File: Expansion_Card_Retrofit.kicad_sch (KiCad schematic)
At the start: 186 parts, among them J4 Conn_02x02_Odd_Even, P1 1054440011, Q1 CSD25480F3, SW1 KXT 331 LHS, SW2 KXT 331 LHS, U1 TXS0202YZPR, U10 TMP110D, U11 MMC5633NJL, U12 STM32L422RBIx, U2 CCGM1A1, U3 TVS0500DRV, U4 W25Q16JLUXIG TR, U5 USB3740B-AI2, U9 ISM330DHCX, Y1 S3A2505-100.000-L-X1-R

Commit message: testbench done
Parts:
- removed U3: TVS0500DRV, Package_SON:WSON-6-1EP_2x2mm_P0.65mm_EP1x1.6mm, symbol Power_Protection:TVS0500DRV
- added C119: 1u, Capacitor_SMD:C_0402_1005Metric, symbol Device:C
- added D17: PTVS5V0Z1USK, Diode_SMD:Nexperia_DSN1608-2_1.6x0.8mm, symbol Diode:PTVS5V0Z1USK
- added R50, R53: 5K1, Resistor_SMD:R_0201_0603Metric, symbol Device:R_US
- R4: now not fitted; now left out of the parts list
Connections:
- net TX1 is gone; now on net RX0: U2.D17 (IO_EB_B2)
- net +2V5: now also C119.1, R50.1
- net GND: now also C119.2, D17.2 (A), R53.2
- net VBUS_UNPROTECTED: now also D17.1 (K)
- net ~{FPGA_RST}: now also R53.1
- net ~{RST}: now also R50.2
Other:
- moved on the sheet: C46, C47, R12, U4

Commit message: fixed diff pair
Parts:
- U12: value STM32L422RBIx -> STM32L422RBI6

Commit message: RevA
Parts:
- added D7: 16-213SDRC/S530-A3/TR8, LED_SMD:LED_0402_1005Metric, symbol Device:LED
- added R20: 60R4, Resistor_SMD:R_0201_0603Metric, symbol Device:R_US
- C1: renamed from C125; MPN (none) -> C0402C104K8PACTU
- C10: renamed from C78; MPN (none) -> C0402C104K8PACTU
- C11: renamed from C79; MPN (none) -> CL05A105KA5NQNC
- C12: renamed from C80; MPN (none) -> C0402C104K8PACTU
- C13: renamed from C46; MPN (none) -> C0201C103K4PACTU
- C14: renamed from C47; MPN (none) -> C0402C104K8PACTU
- C15: renamed from C119; MPN (none) -> CL05A105KA5NQNC
- C16: renamed from C1; MPN (none) -> C0402C104K8PACTU
- C17: renamed from C2; MPN (none) -> C0402C104K8PACTU
- C18: renamed from C3; MPN (none) -> C0402C104K8PACTU
- C19: renamed from C65; MPN (none) -> CL05A105KA5NQNC
- C2: renamed from C48; MPN (none) -> C0201C103K4PACTU
- C20: renamed from C66; MPN (none) -> C0402C104K8PACTU
- C21: renamed from C67; MPN (none) -> C0201C103K4PACTU
- C22: renamed from C68; MPN (none) -> C0201C103K4PACTU
- C23: renamed from C69; MPN (none) -> C0201C103K4PACTU
- C24: renamed from C70; MPN (none) -> C0201C103K4PACTU
- C25: renamed from C71; MPN (none) -> C0201C103K4PACTU
- C26: renamed from C72; MPN (none) -> C0201C103K4PACTU
- C27: renamed from C73; MPN (none) -> C0402C104K8PACTU
- C28: renamed from C74; MPN (none) -> CL05A105KA5NQNC
- C29: renamed from C81; MPN (none) -> C0402C104K8PACTU
- C3: renamed from C49; MPN (none) -> C0201C103K4PACTU
- C30: renamed from C118; MPN (none) -> C0402C104K8PACTU
- C31: renamed from C40; MPN (none) -> CL05A105KA5NQNC
- C32: renamed from C39; MPN (none) -> C0402C104K8PACTU
- C33: renamed from C38; MPN (none) -> C0201C103K4PACTU
- C34: renamed from C37; MPN (none) -> C0201C103K4PACTU
- C35: renamed from C36; MPN (none) -> C0201C103K4PACTU
- C36: renamed from C18; MPN (none) -> CL05A105KA5NQNC
- C37: renamed from C17; MPN (none) -> C0402C104K8PACTU
- C38: renamed from C16; MPN (none) -> C0201C103K4PACTU
- C39: renamed from C19; MPN (none) -> C0201C103K4PACTU
- C4: renamed from C50; MPN (none) -> C0201C103K4PACTU
- C40: renamed from C20; MPN (none) -> C0201C103K4PACTU
- C41: renamed from C25; MPN (none) -> C0201C103K4PACTU
- C42: renamed from C24; MPN (none) -> C0201C103K4PACTU
- C43: renamed from C23; MPN (none) -> C0201C103K4PACTU
- C44: renamed from C22; MPN (none) -> C0402C104K8PACTU
- C45: renamed from C21; MPN (none) -> CL05A105KA5NQNC
- C46: renamed from C26; MPN (none) -> CL05A105KA5NQNC
- C47: renamed from C27; MPN (none) -> C0402C104K8PACTU
- C48: renamed from C28; MPN (none) -> C0201C103K4PACTU
- C49: renamed from C29; MPN (none) -> C0201C103K4PACTU
- C5: renamed from C51; MPN (none) -> C0201C103K4PACTU
- C50: renamed from C30; MPN (none) -> C0201C103K4PACTU
- C51: renamed from C31; MPN (none) -> C0201C103K4PACTU
- C52: renamed from C32; MPN (none) -> C0201C103K4PACTU
- C53: renamed from C33; MPN (none) -> C0201C103K4PACTU
- C54: renamed from C34; MPN (none) -> C0402C104K8PACTU
- C55: renamed from C35; MPN (none) -> CL05A105KA5NQNC
- C56: renamed from C45; MPN (none) -> C0201C103K4PACTU
- C57: renamed from C44; MPN (none) -> C0201C103K4PACTU
- C58: renamed from C43; MPN (none) -> C0201C103K4PACTU
- C59: renamed from C42; MPN (none) -> C0402C104K8PACTU
- C6: renamed from C54; MPN (none) -> C0201C103K4PACTU
- C60: renamed from C41; MPN (none) -> CL05A105KA5NQNC
- C61: renamed from C9; MPN (none) -> C0402C104K8PACTU
- C62: renamed from C10; MPN (none) -> C0402C104K8PACTU
- C63: MPN (none) -> C0201C103K4PACTU
- C64: renamed from C89; MPN (none) -> C0402C104K8PACTU
- C65: renamed from C90; MPN (none) -> CL05A105KA5NQNC
- C66: renamed from C64; MPN (none) -> C0201C103K4PACTU
- C67: renamed from C82; MPN (none) -> C0201C103K4PACTU
- C68: renamed from C99; MPN (none) -> C0402C104K8PACTU
- C69: renamed from C100; MPN (none) -> C0402C104K8PACTU
- C7: renamed from C75; MPN (none) -> C0201C103K4PACTU
- C70: renamed from C101; MPN (none) -> C0402C104K8PACTU
- C71: renamed from C102; MPN (none) -> C0402C104K8PACTU
- C72: renamed from C103; MPN (none) -> C0402C104K8PACTU
- C73: renamed from C104; MPN (none) -> C0402C104K8PACTU
- C74: renamed from C105; MPN (none) -> C0402C104K8PACTU
- C75: renamed from C106; MPN (none) -> C0402C104K8PACTU
- C76: renamed from C107; MPN (none) -> CL05A105KA5NQNC
- C77: renamed from C108; MPN (none) -> CL05A105KA5NQNC
- C78: renamed from C109; MPN (none) -> CL05A105KA5NQNC
- C79: renamed from C110; MPN (none) -> CL05A105KA5NQNC
- C8: renamed from C76; MPN (none) -> C0201C103K4PACTU
- C80: renamed from C11; MPN (none) -> C0201C103K4PACTU
- C81: renamed from C12; MPN (none) -> C0402C104K8PACTU
- C82: renamed from C13; MPN (none) -> CL05A105KA5NQNC
- C83: renamed from C53; MPN (none) -> C0201C103K4PACTU
- C84: renamed from C91; MPN (none) -> C0201C103K4PACTU
- C85: renamed from C92; MPN (none) -> C0201C103K4PACTU
- C86: renamed from C93; MPN (none) -> C0201C103K4PACTU
- C87: renamed from C94; MPN (none) -> C0201C103K4PACTU
- C88: renamed from C95; MPN (none) -> C0201C103K4PACTU
- C89: renamed from C96; MPN (none) -> C0201C103K4PACTU
- C9: renamed from C77; MPN (none) -> C0201C103K4PACTU
- C90: renamed from C97; MPN (none) -> C0201C103K4PACTU
- C91: renamed from C98; MPN (none) -> C0201C103K4PACTU
- C92: renamed from C111; MPN (none) -> C0201C103K4PACTU
- C93: renamed from C112; MPN (none) -> C0201C103K4PACTU
- C94: renamed from C113; MPN (none) -> C0201C103K4PACTU
- C95: renamed from C114; MPN (none) -> C0201C103K4PACTU
- C96: renamed from C115; MPN (none) -> C0201C103K4PACTU
- C97: renamed from C116; MPN (none) -> C0201C103K4PACTU
- C98: renamed from C117; MPN (none) -> C0201C103K4PACTU
- C99: renamed from C52; MPN (none) -> C0402C104K8PACTU
- JP1: MPN (none) -> DNP; now left out of the parts list
- Q1: MPN (none) -> CSD25480F3
- R1: renamed from R13; MPN (none) -> RC0201FR-0760R4L
- R10: renamed from R23; MPN (none) -> RC0201FR-135K1L
- R11: renamed from R38; MPN (none) -> RC0201FR-135K1L
- R12: renamed from R39; MPN (none) -> RC0201FR-135K1L
- R13: renamed from R52; MPN (none) -> RC0201FR-135K1L
- R14: renamed from R2; MPN (none) -> RC0201FR-135K1L
- R15: renamed from R48; MPN (none) -> RC0201FR-135K1L
- R16: renamed from R49; MPN (none) -> RC0201FR-135K1L
- R17: renamed from R21; MPN (none) -> CRCW0201200RFKED
- R18: renamed from R29; MPN (none) -> CR0201AJ/-000GAS
- R19: renamed from R30; MPN (none) -> CR0201AJ/-000GAS
- R2: renamed from R47; MPN (none) -> RC0201FR-135K1L
- R21: renamed from R26; MPN (none) -> CR0201AJ/-000GAS
- R22: renamed from R27; MPN (none) -> CR0201AJ/-000GAS
- R23: renamed from R5; MPN (none) -> RC0201FR-0760R4L
- R24: renamed from R19; MPN (none) -> RC0201FR-135K1L
- R25: renamed from R20; MPN (none) -> RC0201FR-135K1L
- R26: renamed from R6; MPN (none) -> RC0201FR-0760R4L
- R27: renamed from R28; MPN (none) -> CRCW0201200RFKED
- R28: renamed from R7; MPN (none) -> RC0201FR-0760R4L
- R29: renamed from R25; MPN (none) -> CRCW0201200RFKED
- R3: renamed from R14; MPN (none) -> RC0201FR-0760R4L
- R30: renamed from R43; MPN (none) -> RC0201FR-135K1L
- R31: renamed from R44; MPN (none) -> RC0201FR-135K1L
- R32: renamed from R8; MPN (none) -> RC0201FR-0760R4L
- R33: MPN (none) -> CR0201AJ/-000GAS
- R34: renamed from R32; MPN (none) -> CR0201AJ/-000GAS
- R35: renamed from R36; MPN (none) -> RC0201FR-0760R4L
- R36: renamed from R17; MPN (none) -> RC0201FR-135K1L
- R37: MPN (none) -> RC0201FR-0760R4L
- R38: renamed from R46; MPN (none) -> CR0201AJ/-000GAS
- R39: renamed from R41; MPN (none) -> RC0201FR-135K1L
- R4: renamed from R50; MPN (none) -> RC0201FR-135K1L
- R40: renamed from R42; MPN (none) -> RC0201FR-135K1L
- R41: renamed from R51; MPN (none) -> RC0201FR-071K5L
- R42: renamed from R15; MPN (none) -> RC0201FR-135K1L
- R43: renamed from R31; MPN (none) -> RC0201FR-07100RL
- R44: renamed from R4; MPN (none) -> RC0201FR-135K1L
- R45: renamed from R16; MPN (none) -> CR0201AJ/-000GAS
- R46: renamed from R22; MPN (none) -> RC0201FR-07100RL
- R47: renamed from R53; MPN (none) -> RC0201FR-135K1L
- R5: renamed from R34; MPN (none) -> CR0201AJ/-000GAS
- R6: renamed from R3; MPN (none) -> RC0201FR-135K1L
- R7: renamed from R18; MPN (none) -> RC0201FR-135K1L
- R8: renamed from R12; MPN (none) -> RC0201FR-135K1L
- R9: renamed from R45; MPN (none) -> CR0201AJ/-000GAS
- SW1, SW2: MPN (none) -> KXT 331 LHS
- TP1: renamed from TP7; MPN (none) -> DNP
- TP2: renamed from TP8; MPN (none) -> DNP
- TP3: renamed from TP5; MPN (none) -> DNP
- TP4: renamed from TP6; MPN (none) -> DNP
- TP5: renamed from TP1; MPN DNP -> DNP
- TP6: renamed from TP2; MPN DNP -> DNP
- TP7: renamed from TP3; MPN DNP -> DNP
- TP8: renamed from TP4; MPN DNP -> DNP
- U4: renamed from U12; MPN (none) -> STM32L422RBI6
- U5: renamed from U1; MPN (none) -> TXS0202YZPR
- renumbered D17 to D1, D3 to D10, D4 to D11, D5 to D12, D6 to D13, D10 to D2, D11 to D3, D16 to D4, D15 to D5, D9 to D6, D1 to D8, D2 to D9, FID5 to FID3, FID3 to FID4, FID4 to FID5, J4 to J1, U5 to U1, U4 to U2, U2 to U3, U11 to U6, U10 to U7, U9 to U8
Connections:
- net GND: now also R20.1
- net ~{FPGA_RST}: now also D7.2 (A)
- new net: D7.1 (K), R20.2
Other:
- moved on the sheet: R45, U3G

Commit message: add readme
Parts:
- added U12: MCP2210x-MQ, Package_DFN_QFN:QFN-20-1EP_5x5mm_P0.65mm_EP3.35x3.35mm, symbol Interface_USB:MCP2210x-MQ
- added U13: FXMA108, Package_DFN_QFN:WQFN-20-1EP_2.5x4.5mm_P0.5mm_EP1x2.9mm, symbol Logic_LevelTranslator:FXMA108
- U7: value TMP110D -> TMP110D1IDPWR

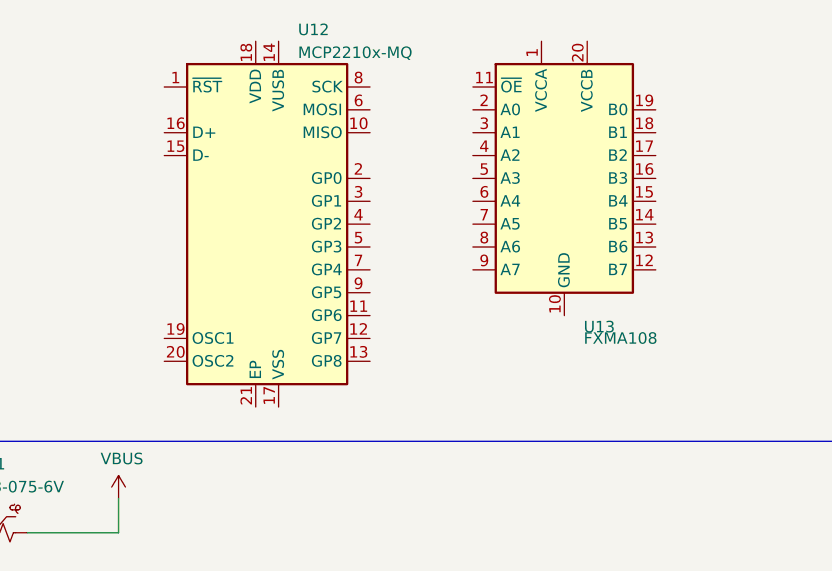
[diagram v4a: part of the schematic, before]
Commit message: add stackup to readme
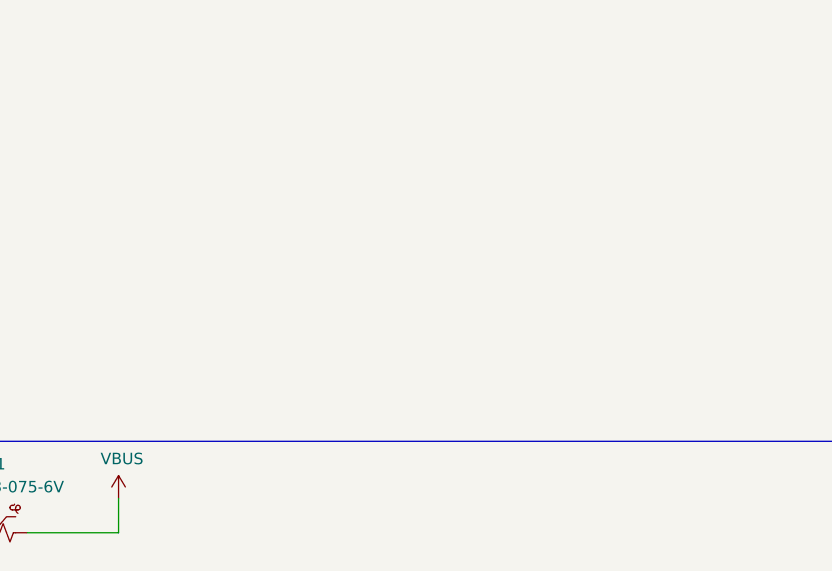
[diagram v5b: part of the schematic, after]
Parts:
- removed U12: MCP2210x-MQ, Package_DFN_QFN:QFN-20-1EP_5x5mm_P0.65mm_EP3.35x3.35mm, symbol Interface_USB:MCP2210x-MQ
- removed U13: FXMA108, Package_DFN_QFN:WQFN-20-1EP_2.5x4.5mm_P0.5mm_EP1x2.9mm, symbol Logic_LevelTranslator:FXMA108
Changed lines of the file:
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@@
 	)
 	(symbol
-		(lib_id "Logic_LevelTranslator:FXMA108")
-		(at 163.83 -16.51 0)
-		(unit 1)
-		(exclude_from_sim no)
-		(in_bom yes)
-		(on_board yes)
-		(dnp no)
-		(fields_autoplaced yes)
-		(property "Reference" "U13"
-			(at 165.9733 0 0)
-			(effects
-				(font
-					(size 1.27 1.27)
-				)
-				(justify left)
-			)
-		)
-		(property "Value" "FXMA108"
-			(at 165.9733 1.27 0)
-			(effects
-				(font
-					(size 1.27 1.27)
-				)
-				(justify left)
-			)
-		)
-		(property "Footprint" "Package_DFN_QFN:WQFN-20-1EP_2.5x4.5mm_P0.5mm_EP1x2.9mm"
-			(at 163.83 1.27 0)
-			(effects
-				(font
-					(size 1.27 1.27)
-				)
-				(hide yes)
-			)
-		)
-		(property "Datasheet" "http://www.onsemi.com/pub/Collateral/FXMA108-D.pdf"
-			(at 163.83 -17.78 0)
-			(effects
-				(font
-					(size 1.27 1.27)
-				)
-				(hide yes)
-			)
-		)
-		(property "Description" "Dual-Supply, 8-Bit Signal Translator with Configurable Voltage Supplies and Signals Levels, 3-State Outputs and Auto Direction Sensing, WQFN-20"
-			(at 163.83 -16.51 0)
-			(effects
-				(font
-					(size 1.27 1.27)
-				)
-				(hide yes)
-			)
-		)
-		(pin "15"
-		)
-		(pin "19"
-		)
-		(pin "20"
-		)
-		(pin "10"
-		)
-		(pin "13"
-		)
-		(pin "12"
-		)
-		(pin "1"
-		)
-		(pin "14"
-		)
-		(pin "9"
-		)
-		(pin "8"
-		)
-		(pin "5"
-		)
-		(pin "2"
-		)
-		(pin "4"
-		)
-		(pin "6"
-		)
-		(pin "18"
-		)
-		(pin "16"
-		)
-		(pin "21"
-		)
-		(pin "17"
-		)
-		(pin "7"
-		)
-		(pin "11"
-		)
-		(pin "3"
-		)
-		(instances
-			(project ""
-				(path "/f3b918d3-9afe-4ecb-86cc-12f1996b3981"
-					(reference "U13")
-					(unit 1)
-				)
-			)
-		)
-	)
-	(symbol
 		(lib_id "power:GND")
 		(at 161.29 262.89 0)
@@
 					(unit 1)
 				)
-			)
-		)
-	)
-	(symbol
-		(lib_id "Interface_USB:MCP2210x-MQ")
-		(at 132.08 -11.43 0)
-		(unit 1)
-		(exclude_from_sim no)
-		(in_bom yes)
-		(on_board yes)
-		(dnp no)
-		(fields_autoplaced yes)
-		(property "Reference" "U12"
-			(at 134.2233 -33.02 0)
-			(effects
-				(font
-					(size 1.27 1.27)
-				)
-				(justify left)
-			)
-		)
-		(property "Value" "MCP2210x-MQ"
-			(at 134.2233 -30.48 0)
-			(effects
-				(font
-					(size 1.27 1.27)
-				)
-				(justify left)
-			)
-		)
-		(property "Footprint" "Package_DFN_QFN:QFN-20-1EP_5x5mm_P0.65mm_EP3.35x3.35mm"
-			(at 132.08 -36.83 0)
-			(effects
-				(font
-					(size 1.27 1.27)
-				)
-				(hide yes)
-			)
-		)
-		(property "Datasheet" "https://ww1.microchip.com/downloads/en/DeviceDoc/22288A.pdf"
-			(at 129.54 -31.75 0)
-			(effects
-				(font
-					(size 1.27 1.27)
-				)
-				(hide yes)
-			)
-		)
-		(property "Description" "USB to SPI Protocol Converter with GPIO, QFN-20"
-			(at 132.08 -11.43 0)
-			(effects
-				(font
-					(size 1.27 1.27)
-				)
-				(hide yes)
-			)
-		)
-		(pin "3"
-		)
-		(pin "4"
-		)
-		(pin "7"
-		)
-		(pin "17"
-		)
-		(pin "5"
-		)
-		(pin "11"
-		)
-		(pin "20"
-		)
-		(pin "8"
-		)
-		(pin "6"
-		)
-		(pin "12"
-		)
-		(pin "13"
-		)
-		(pin "19"
-		)
-		(pin "16"
-		)
-		(pin "18"
-		)
-		(pin "21"
-		)
-		(pin "1"
-		)
-		(pin "15"
-		)
-		(pin "14"
-		)
-		(pin "9"
-		)
-		(pin "2"
-		)
-		(pin "10"
-		)
-		(instances
-			(project ""
-				(path "/f3b918d3-9afe-4ecb-86cc-12f1996b3981"
-					(reference "U12")
-					(unit 1)
-				)
